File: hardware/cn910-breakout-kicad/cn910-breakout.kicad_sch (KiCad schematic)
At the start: 30 parts, among them J1 CN910, J2 USB4125-GF-A-0190_REVA2, J3 PB_RF_OUT, SW1 SW_SPDT, U1 ADA4857-1YRZ

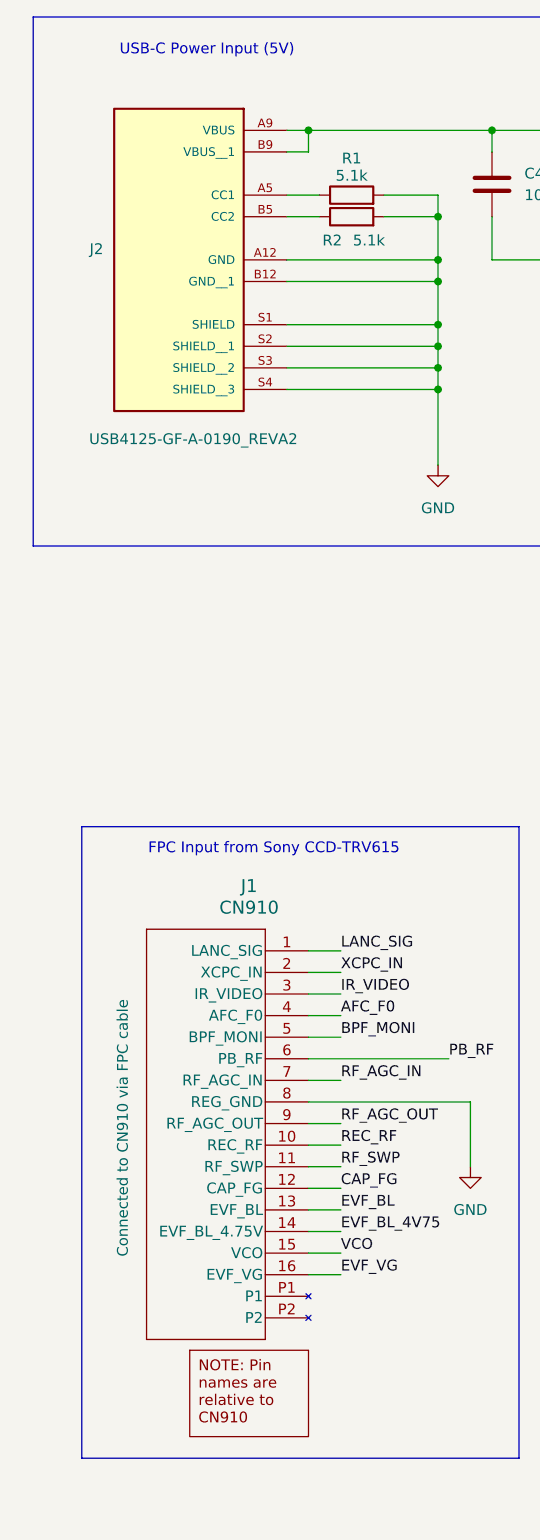
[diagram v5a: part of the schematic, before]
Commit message: Updated CN910 breakout KiCad project files with dynamic project metadata, including title, company, version, and license. Refined design rules and component properties for improved clarity and organization. Adjusted pin functions and descriptions for connectors, and removed obsolete library references. Enhanced layout with new wire connections and updated schematic components.
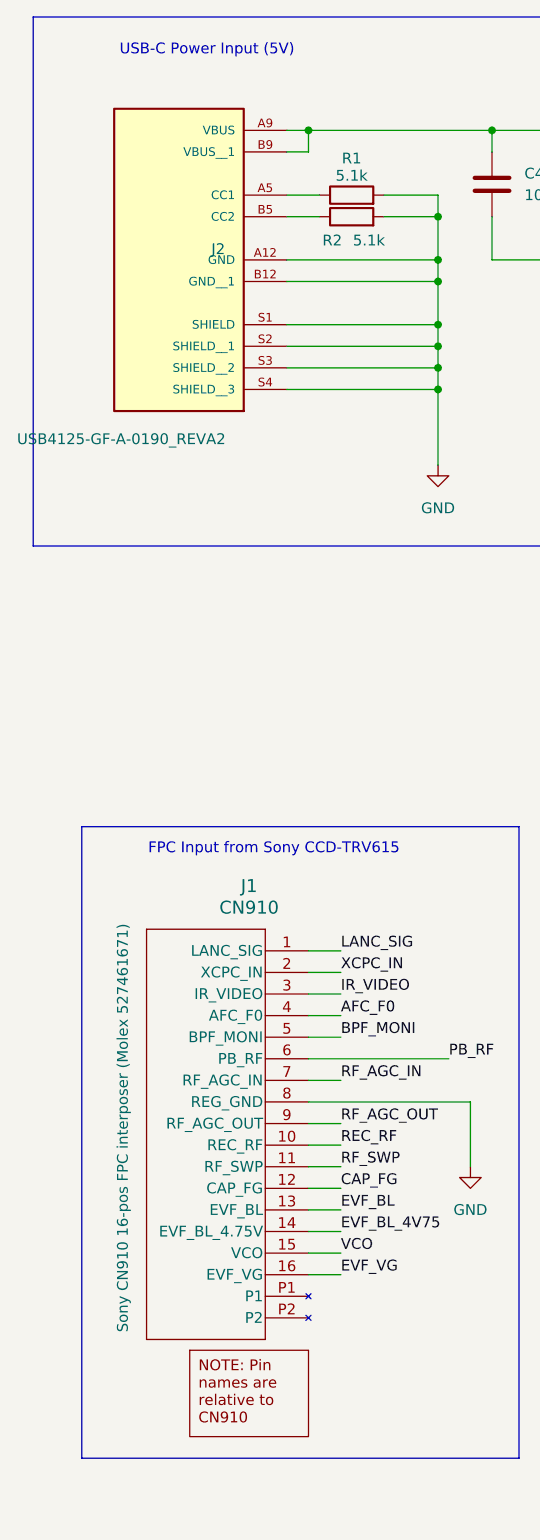
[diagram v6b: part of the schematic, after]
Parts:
- J1: MPN (none) -> 527461671; Manufacturer (none) -> Molex
- J2: MPN (none) -> USB4125-GF-A-0190; Manufacturer (none) -> GCT
- J3: now in the parts list
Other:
- company: GDH Technologies LLC -> ${proj-company}
- title: Sony CCD-TRV615 ADA4857 Amp -> ${proj-title}
